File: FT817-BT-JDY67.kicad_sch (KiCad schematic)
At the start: 23 parts, among them J1009 Mini-DIN-8PR, J1010 Mini-DIN-6PR, U1 JDY-67 Bluetooth Module, U2 LM1117MP-3.3

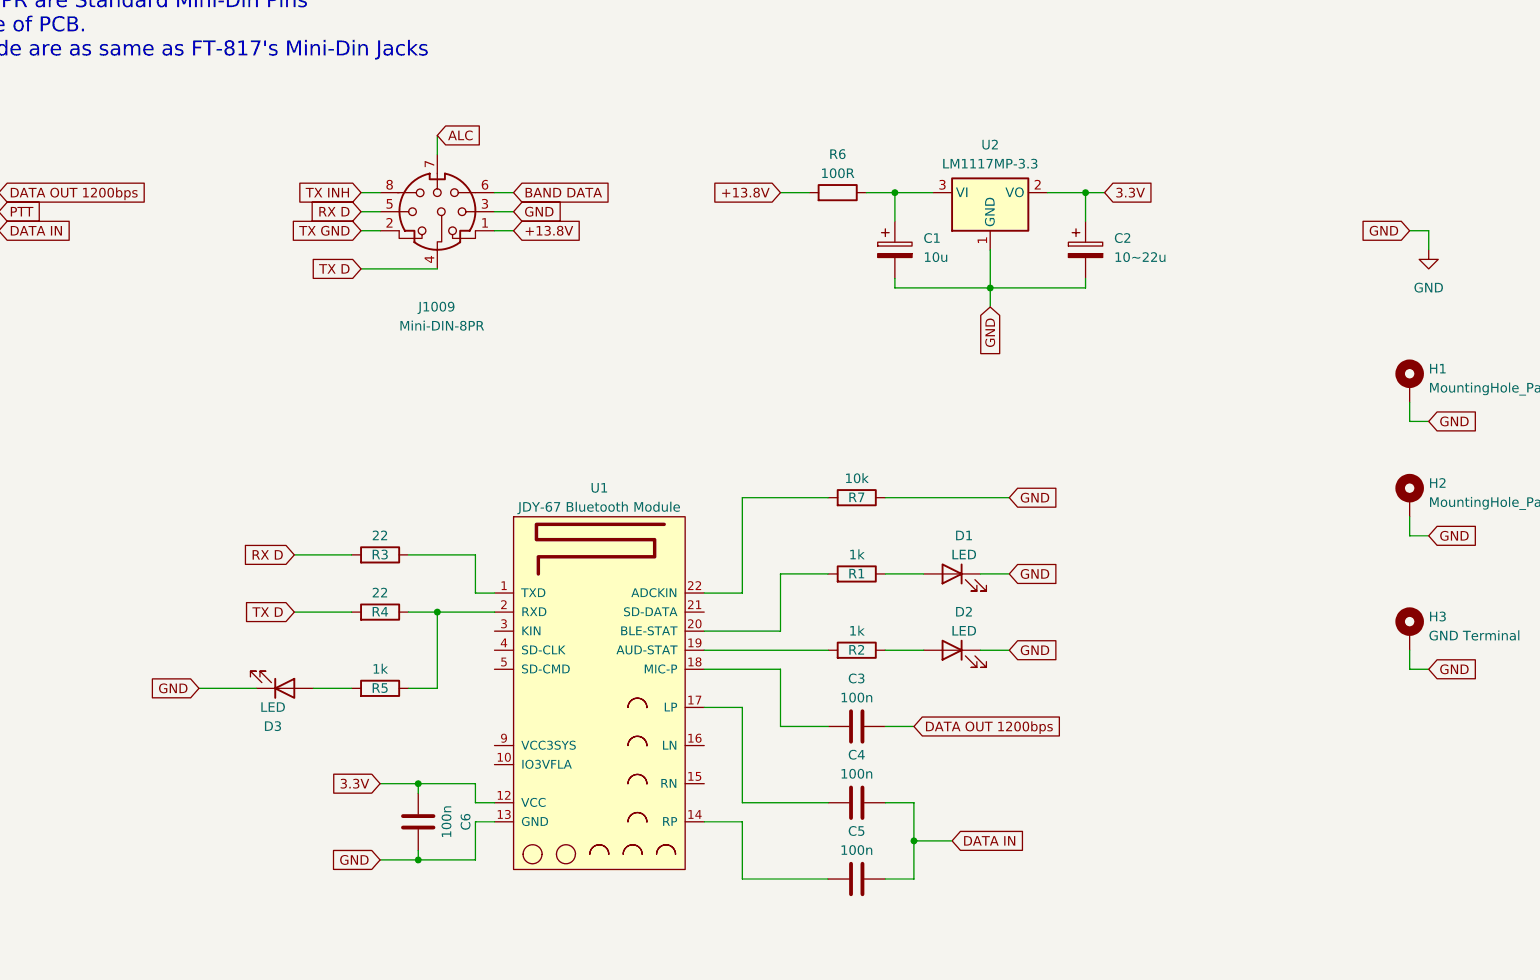
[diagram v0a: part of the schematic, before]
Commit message: 1. Add 6.2V zener for pre-conditioning before LM1117-3.3 2. Add attenuation network for Line->Mic 3. Add EMI inductor on TXD/RXD pins.
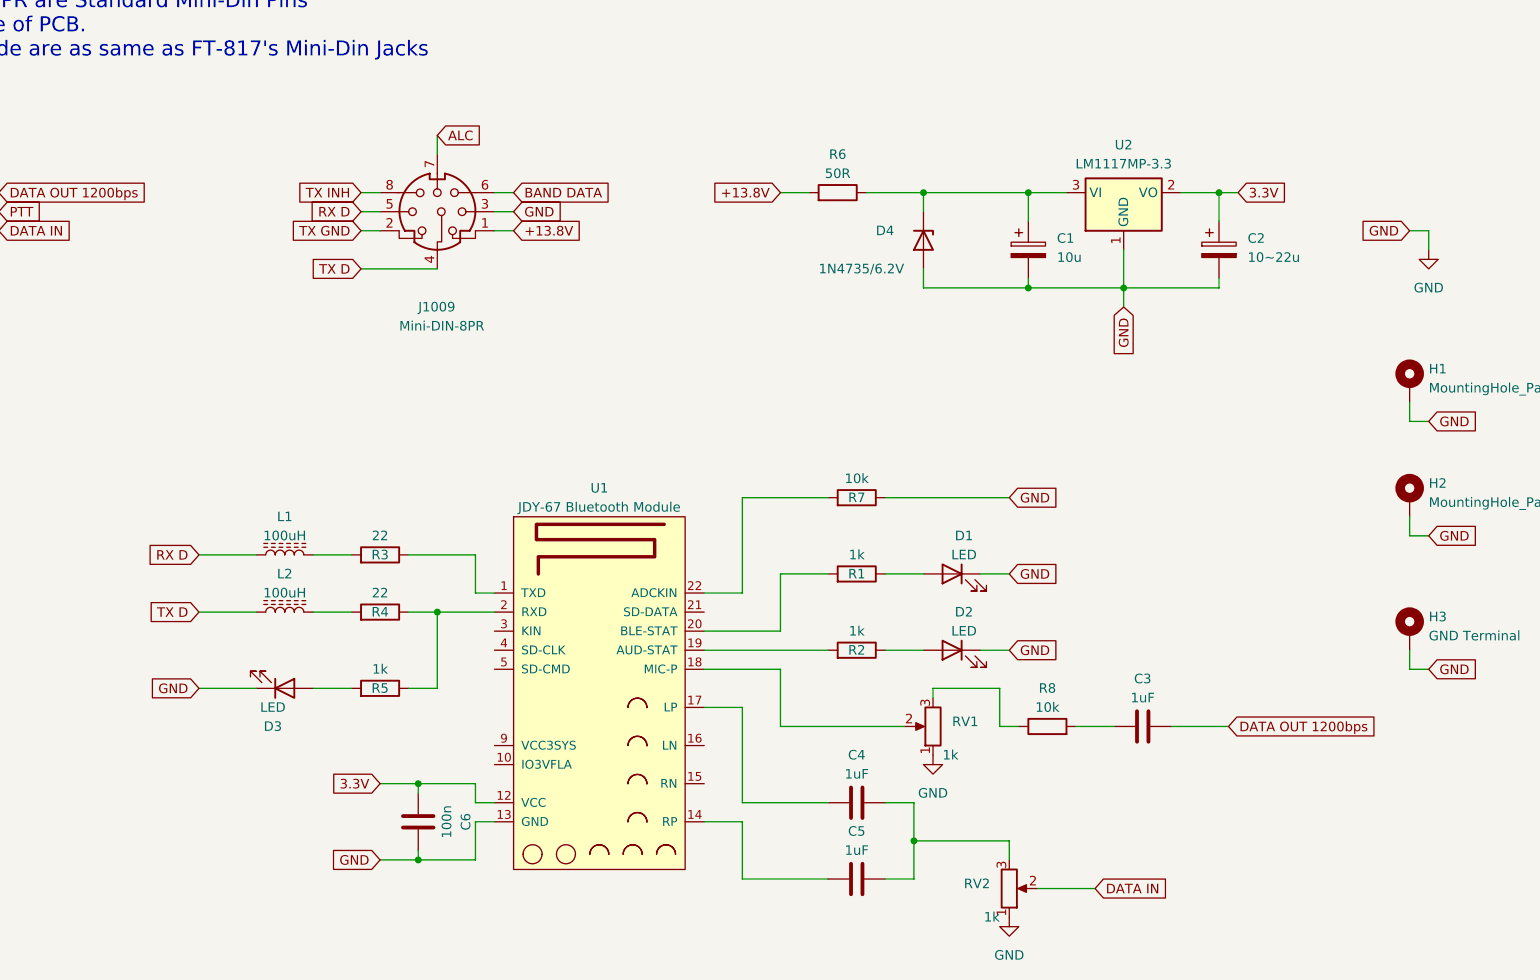
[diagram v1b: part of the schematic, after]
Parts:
- added D4: 1N4735/6.2V, symbol Device:D_Zener
- added L1, L2: 100uH, symbol Device:L_Ferrite
- added R8: 10k, symbol Device:R
- added RV1, RV2: 1k, symbol Device:R_Potentiometer
- C3, C4, C5: value 100n -> 1uF
- R6: value 100R -> 50R
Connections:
- net DATA IN: now also RV2.2; no longer C4.2, C5.2
- net GND: now also D4.2 (A), RV1.1, RV2.1
- net RX D: now also L1.1; no longer R3.2
- net TX D: now also L2.1; no longer R4.2
- net at C3.1: now also R8.2; no longer U1.18 (MIC-P)
- net at C1.1, R6.1, U2.3 (VI): now also D4.1 (K)
- new net: C4.2, C5.2, RV2.3
- new net: RV1.2, U1.18 (MIC-P)
- new net: L2.2, R4.2
- new net: R8.1, RV1.3
- new net: L1.2, R3.2
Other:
- moved on the sheet: C1, C2, C3, U2

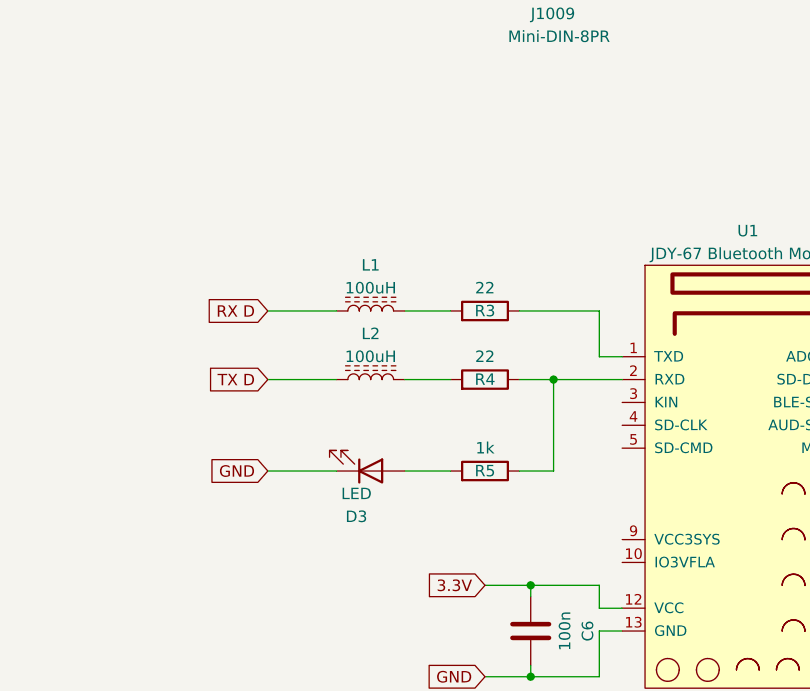
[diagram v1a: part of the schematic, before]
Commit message: Reconnect D3 to RXD
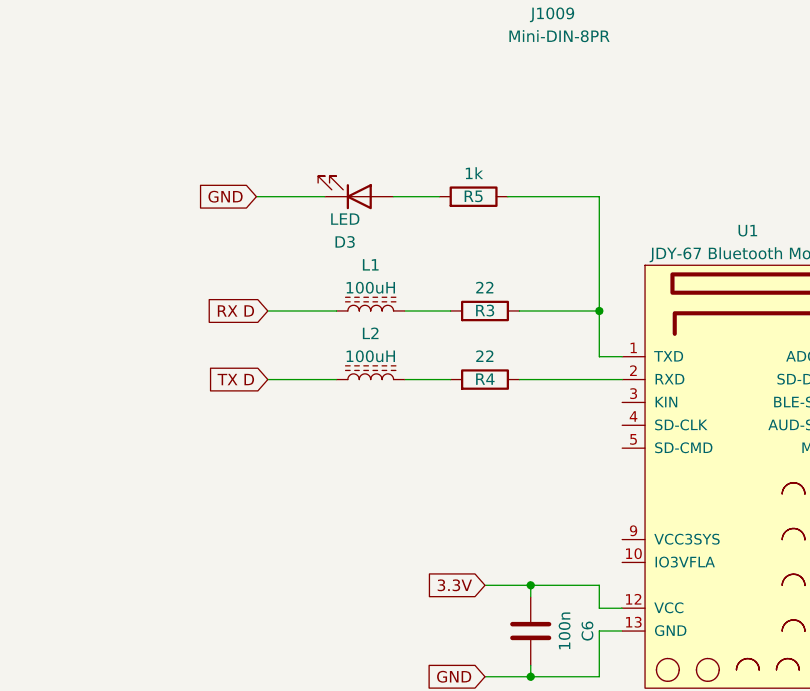
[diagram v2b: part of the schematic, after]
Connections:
- net at R3.1, U1.1 (TXD): now also R5.1
- net at R4.1, U1.2 (RXD): no longer R5.1
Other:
- moved on the sheet: D3, R5
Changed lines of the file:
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@@
   (junction (at 213.36 63.5) (diameter 0) (color 0 0 0 0)
   )
+  (junction (at 127 99.06) (diameter 0) (color 0 0 0 0)
+  )
   (junction (at 119.38 139.7) (diameter 0) (color 0 0 0 0)
   )
-  (junction (at 121.92 106.68) (diameter 0) (color 0 0 0 0)
-  )
   (junction (at 200.66 50.8) (diameter 0) (color 0 0 0 0)
   )
@@
     (stroke (width 0) (type default))
   )
-  (wire (pts (xy 121.92 106.68) (xy 129.54 106.68))
+  (wire (pts (xy 118.11 106.68) (xy 129.54 106.68))
     (stroke (width 0) (type default))
   )
@@
     (stroke (width 0) (type default))
   )
-  (wire (pts (xy 118.11 106.68) (xy 121.92 106.68))
-    (stroke (width 0) (type default))
-  )
   (wire (pts (xy 251.46 81.28) (xy 251.46 78.74))
     (stroke (width 0) (type default))
@@
     (stroke (width 0) (type default))
   )
-  (wire (pts (xy 118.11 116.84) (xy 121.92 116.84))
+  (wire (pts (xy 116.84 86.36) (xy 127 86.36))
     (stroke (width 0) (type default))
   )
@@
     (stroke (width 0) (type default))
   )
-  (wire (pts (xy 121.92 116.84) (xy 121.92 106.68))
-    (stroke (width 0) (type default))
-  )
   (wire (pts (xy 127 134.62) (xy 129.54 134.62))
     (stroke (width 0) (type default))
   )
+  (wire (pts (xy 127 86.36) (xy 127 99.06))
+    (stroke (width 0) (type default))
+  )
   (wire (pts (xy 90.17 106.68) (xy 97.79 106.68))
     (stroke (width 0) (type default))
@@
     (stroke (width 0) (type default))
   )
-  (wire (pts (xy 105.41 116.84) (xy 110.49 116.84))
+  (wire (pts (xy 104.14 86.36) (xy 109.22 86.36))
     (stroke (width 0) (type default))
   )
@@
     (stroke (width 0) (type default))
   )
-  (wire (pts (xy 90.17 116.84) (xy 97.79 116.84))
+  (wire (pts (xy 88.9 86.36) (xy 96.52 86.36))
     (stroke (width 0) (type default))
   )
@@
     )
   )
-  (global_label "GND" (shape input) (at 90.17 116.84 180) (fields_autoplaced)
-    (effects (font (size 1.27 1.27)) (justify right))
-    (property "Intersheetrefs" "${INTERSHEET_REFS}" (at 83.3937 116.84 0)
+  (global_label "GND" (shape input) (at 88.9 86.36 180) (fields_autoplaced)
+    (effects (font (size 1.27 1.27)) (justify right))
+    (property "Intersheetrefs" "${INTERSHEET_REFS}" (at 82.1237 86.36 0)
       (effects (font (size 1.27 1.27)) (justify right) hide)
     )
@@
     )
   )
-  (symbol (lib_id "Device:LED") (at 101.6 116.84 0) (mirror x) (unit 1)
+  (symbol (lib_id "Device:LED") (at 100.33 86.36 0) (mirror x) (unit 1)
     (in_bom yes) (on_board yes) (dnp no)
-    (property "Reference" "D3" (at 100.0125 121.92 0)
-      (effects (font (size 1.27 1.27)))
-    )
-    (property "Value" "LED" (at 100.0125 119.38 0)
-      (effects (font (size 1.27 1.27)))
-    )
-    (property "Footprint" "LED_SMD:LED_0805_2012Metric" (at 101.6 116.84 0)
-      (effects (font (size 1.27 1.27)) hide)
-    )
-    (property "Datasheet" "~" (at 101.6 116.84 0)
+    (property "Reference" "D3" (at 98.7425 91.44 0)
+      (effects (font (size 1.27 1.27)))
+    )
+    (property "Value" "LED" (at 98.7425 88.9 0)
+      (effects (font (size 1.27 1.27)))
+    )
+    (property "Footprint" "LED_SMD:LED_0805_2012Metric" (at 100.33 86.36 0)
+      (effects (font (size 1.27 1.27)) hide)
+    )
+    (property "Datasheet" "~" (at 100.33 86.36 0)
       (effects (font (size 1.27 1.27)) hide)
     )
@@
     )
   )
-  (symbol (lib_id "Device:R") (at 114.3 116.84 270) (mirror x) (unit 1)
+  (symbol (lib_id "Device:R") (at 113.03 86.36 270) (mirror x) (unit 1)
     (in_bom yes) (on_board yes) (dnp no)
-    (property "Reference" "R5" (at 114.3 116.84 90)
-      (effects (font (size 1.27 1.27)))
-    )
-    (property "Value" "1k" (at 114.3 114.3 90)
-      (effects (font (size 1.27 1.27)))
-    )
-    (property "Footprint" "Resistor_SMD:R_0805_2012Metric" (at 114.3 118.618 90)
-      (effects (font (size 1.27 1.27)) hide)
-    )
-    (property "Datasheet" "~" (at 114.3 116.84 0)
-      (effects (font (size 1.27 1.27)) hide)
-    )
+    (property "Reference" "R5" (at 113.03 86.36 90)
+      (effects (font (size 1.27 1.27)))
+    )
+    (property "Value" "1k" (at 113.03 83.82 90)
+      (effects (font (size 1.27 1.27)))
+    )
+    (property "Footprint" "Resistor_SMD:R_0805_2012Metric" (at 113.03 88.138 90)
+      (effects (font (size 1.27 1.27)) hide)
+    )
+    (property "Datasheet" "~" (at 113.03 86.36 0)
+      (effects (font (size 1.27 1.27)) hide)
+    )

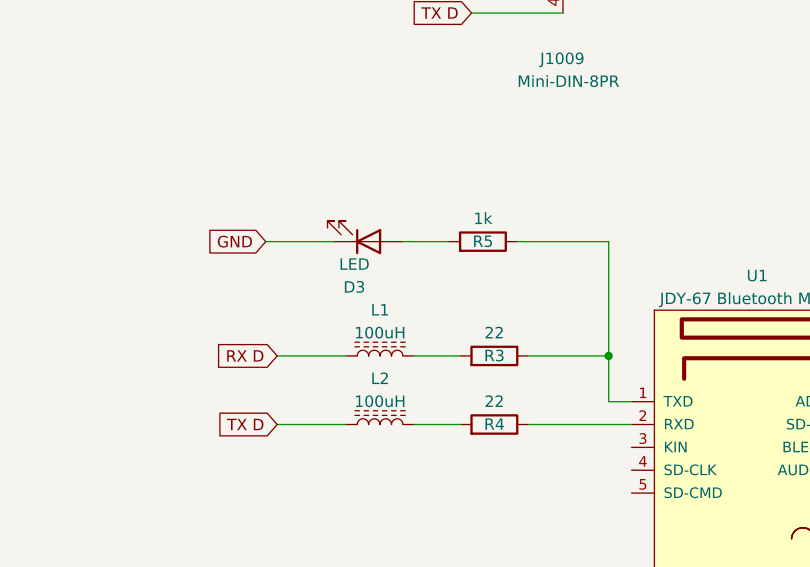
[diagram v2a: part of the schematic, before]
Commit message: Updated footprint for new components.
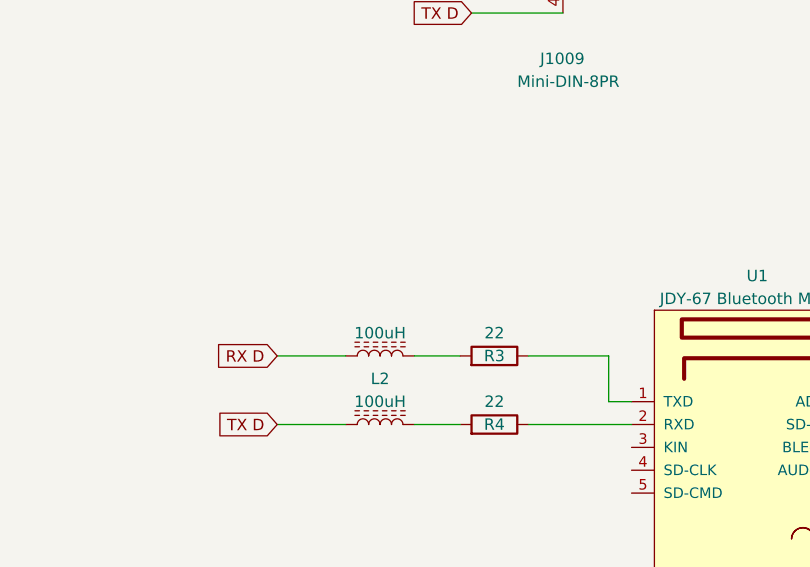
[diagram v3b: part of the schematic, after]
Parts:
- removed D3: LED, LED_SMD:LED_0805_2012Metric, symbol Device:LED
- removed R5: 1k, Resistor_SMD:R_0805_2012Metric, symbol Device:R
- D4: footprint (none) -> Diode_SMD:D_SMA
- L1, L2: footprint (none) -> Inductor_SMD:L_0805_2012Metric_Pad1.05x1.20mm_HandSolder
- RV1, RV2: footprint (none) -> Potentiometer_SMD:Potentiometer_Bourns_3314J_Vertical
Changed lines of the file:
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@@
   (junction (at 213.36 63.5) (diameter 0) (color 0 0 0 0)
   )
-  (junction (at 127 99.06) (diameter 0) (color 0 0 0 0)
-  )
   (junction (at 119.38 139.7) (diameter 0) (color 0 0 0 0)
   )
@@
     (stroke (width 0) (type default))
   )
-  (wire (pts (xy 116.84 86.36) (xy 127 86.36))
-    (stroke (width 0) (type default))
-  )
   (wire (pts (xy 200.66 63.5) (xy 213.36 63.5))
     (stroke (width 0) (type default))
@@
     (stroke (width 0) (type default))
   )
-  (wire (pts (xy 127 86.36) (xy 127 99.06))
-    (stroke (width 0) (type default))
-  )
   (wire (pts (xy 90.17 106.68) (xy 97.79 106.68))
     (stroke (width 0) (type default))
@@
     (stroke (width 0) (type default))
   )
-  (wire (pts (xy 104.14 86.36) (xy 109.22 86.36))
-    (stroke (width 0) (type default))
-  )
   (wire (pts (xy 251.46 114.3) (xy 254 114.3))
     (stroke (width 0) (type default))
@@
   )
   (wire (pts (xy 220.98 50.8) (xy 226.06 50.8))
-    (stroke (width 0) (type default))
-  )
-  (wire (pts (xy 88.9 86.36) (xy 96.52 86.36))
     (stroke (width 0) (type default))
   )
@@
     (effects (font (size 1.27 1.27)) (justify right))
     (property "Intersheetrefs" "${INTERSHEET_REFS}" (at 101.839 55.88 0)
-      (effects (font (size 1.27 1.27)) (justify right) hide)
-    )
-  )
-  (global_label "GND" (shape input) (at 88.9 86.36 180) (fields_autoplaced)
-    (effects (font (size 1.27 1.27)) (justify right))
-    (property "Intersheetrefs" "${INTERSHEET_REFS}" (at 82.1237 86.36 0)
       (effects (font (size 1.27 1.27)) (justify right) hide)
     )
@@
       (effects (font (size 1.27 1.27)) (justify right))
     )
-    (property "Footprint" "" (at 198.12 143.51 0)
+    (property "Footprint" "Potentiometer_SMD:Potentiometer_Bourns_3314J_Vertical" (at 198.12 143.51 0)
       (effects (font (size 1.27 1.27)) hide)
     )
@@
     )
   )
-  (symbol (lib_id "Device:LED") (at 100.33 86.36 0) (mirror x) (unit 1)
-    (in_bom yes) (on_board yes) (dnp no)
-    (property "Reference" "D3" (at 98.7425 91.44 0)
-      (effects (font (size 1.27 1.27)))
-    )
-    (property "Value" "LED" (at 98.7425 88.9 0)
-      (effects (font (size 1.27 1.27)))
-    )
-    (property "Footprint" "LED_SMD:LED_0805_2012Metric" (at 100.33 86.36 0)
-      (effects (font (size 1.27 1.27)) hide)
-    )
-    (property "Datasheet" "~" (at 100.33 86.36 0)
-      (effects (font (size 1.27 1.27)) hide)
-    )
-    (pin "1")
-    (pin "2")
-    (instances
-      (project "FT817-BT-JDY67"
-        (path "/cfc49cd5-e50c-4df9-89f0-cc0db7d3dd1c"
-          (reference "D3") (unit 1)
-        )
-      )
-    )
-  )
   (symbol (lib_id "Connector:Mini-DIN-6") (at 53.34 53.34 0) (unit 1)
     (in_bom yes) (on_board yes) (dnp no)
@@
       (effects (font (size 1.27 1.27)))
     )
-    (property "Footprint" "" (at 101.6 106.68 0)
+    (property "Footprint" "Inductor_SMD:L_0805_2012Metric_Pad1.05x1.20mm_HandSolder" (at 101.6 106.68 0)
       (effects (font (size 1.27 1.27)) hide)
     )
@@
         (path "/cfc49cd5-e50c-4df9-89f0-cc0db7d3dd1c"
           (reference "L2") (unit 1)
-        )
-      )
-    )
-  )
-  (symbol (lib_id "Device:R") (at 113.03 86.36 270) (mirror x) (unit 1)
-    (in_bom yes) (on_board yes) (dnp no)
-    (property "Reference" "R5" (at 113.03 86.36 90)
-      (effects (font (size 1.27 1.27)))
-    )
-    (property "Value" "1k" (at 113.03 83.82 90)
-      (effects (font (size 1.27 1.27)))
-    )
-    (property "Footprint" "Resistor_SMD:R_0805_2012Metric" (at 113.03 88.138 90)
-      (effects (font (size 1.27 1.27)) hide)
-    )
-    (property "Datasheet" "~" (at 113.03 86.36 0)
-      (effects (font (size 1.27 1.27)) hide)
-    )
-    (pin "1")
-    (pin "2")
-    (instances
-      (project "FT817-BT-JDY67"
-        (path "/cfc49cd5-e50c-4df9-89f0-cc0db7d3dd1c"
-          (reference "R5") (unit 1)
         )
       )
@@
     (in_bom yes) (on_board yes) (dnp no) (fields_autoplaced)
     (property "Reference" "L1" (at 101.6 93.98 90)
-      (effects (font (size 1.27 1.27)))
+      (effects (font (size 1.27 1.27)) hide)
     )
     (property "Value" "100uH" (at 101.6 96.52 90)
       (effects (font (size 1.27 1.27)))
     )
-    (property "Footprint" "" (at 101.6 99.06 0)
+    (property "Footprint" "Inductor_SMD:L_0805_2012Metric_Pad1.05x1.20mm_HandSolder" (at 101.6 99.06 0)
       (effects (font (size 1.27 1.27)) hide)
     )
@@
       (effects (font (size 1.27 1.27)) (justify right))
     )
-    (property "Footprint" "" (at 187.96 121.92 0)
+    (property "Footprint" "Potentiometer_SMD:Potentiometer_Bourns_3314J_Vertical" (at 187.96 121.92 0)
       (effects (font (size 1.27 1.27)) hide)
     )
@@
       (effects (font (size 1.27 1.27)) (justify left))
     )
-    (property "Footprint" "" (at 186.69 57.15 0)
-      (effects (font (size 1.27 1.27)) hide)
-    )
+    (property "Footprint" "Diode_SMD:D_SMA" (at 186.69 57.15 0)
+      (effects (font (size 1.27 1.27)) hide)
+    )
